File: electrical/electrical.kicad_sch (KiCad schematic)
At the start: 0 parts

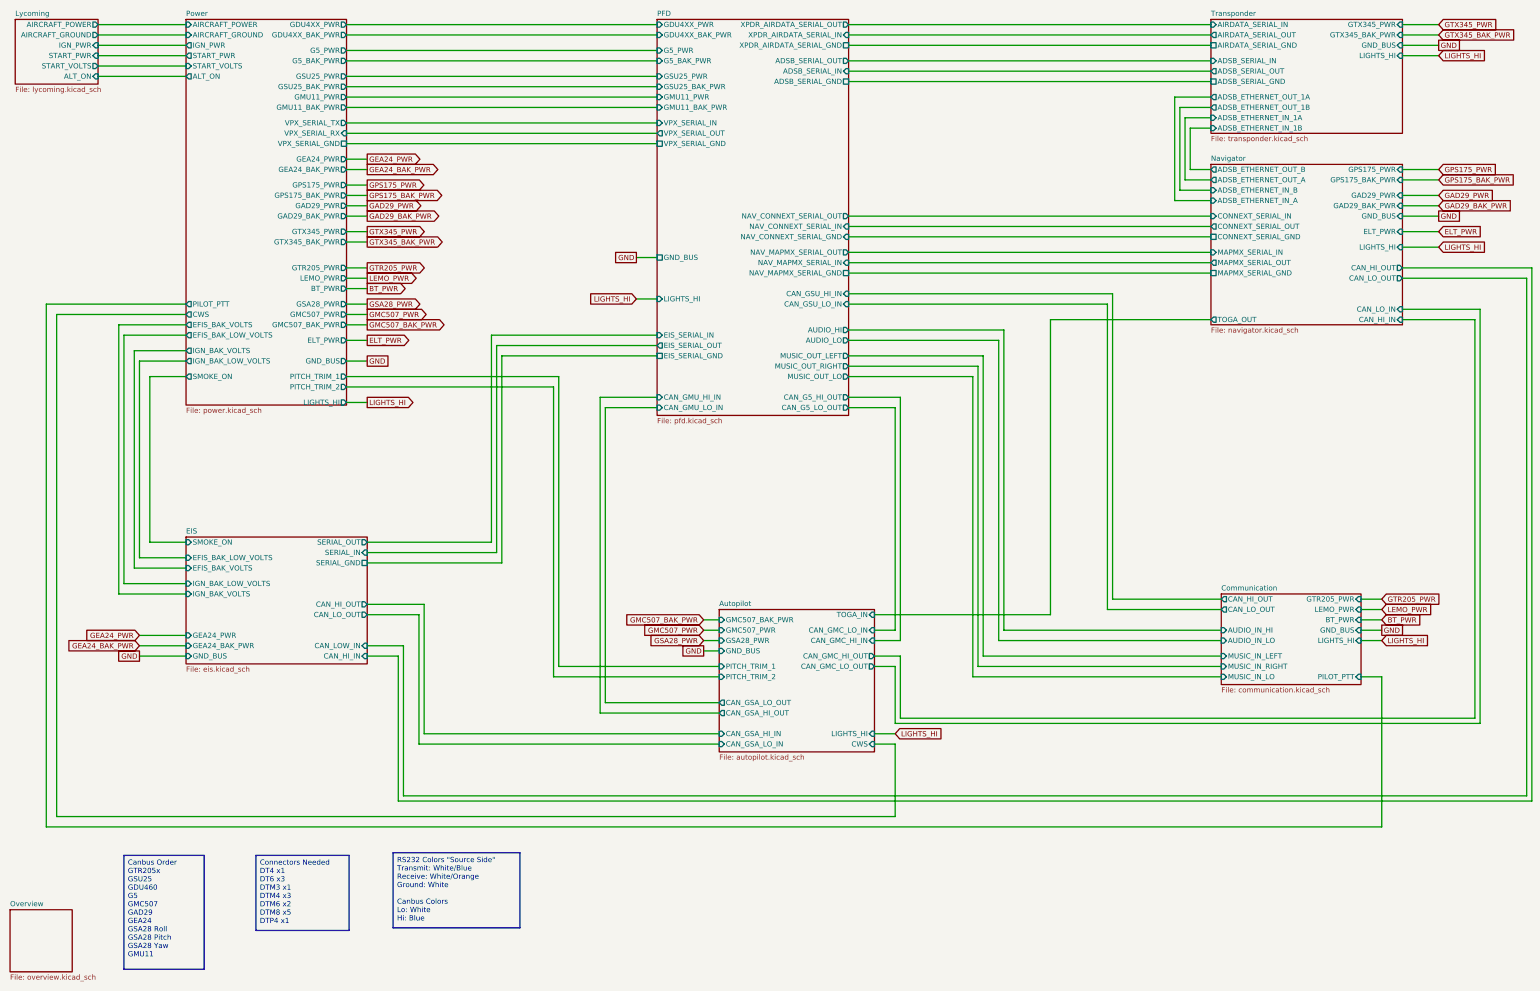
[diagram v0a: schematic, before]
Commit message: Added Rudder Trim and Ray Allen T3 Servo Type.
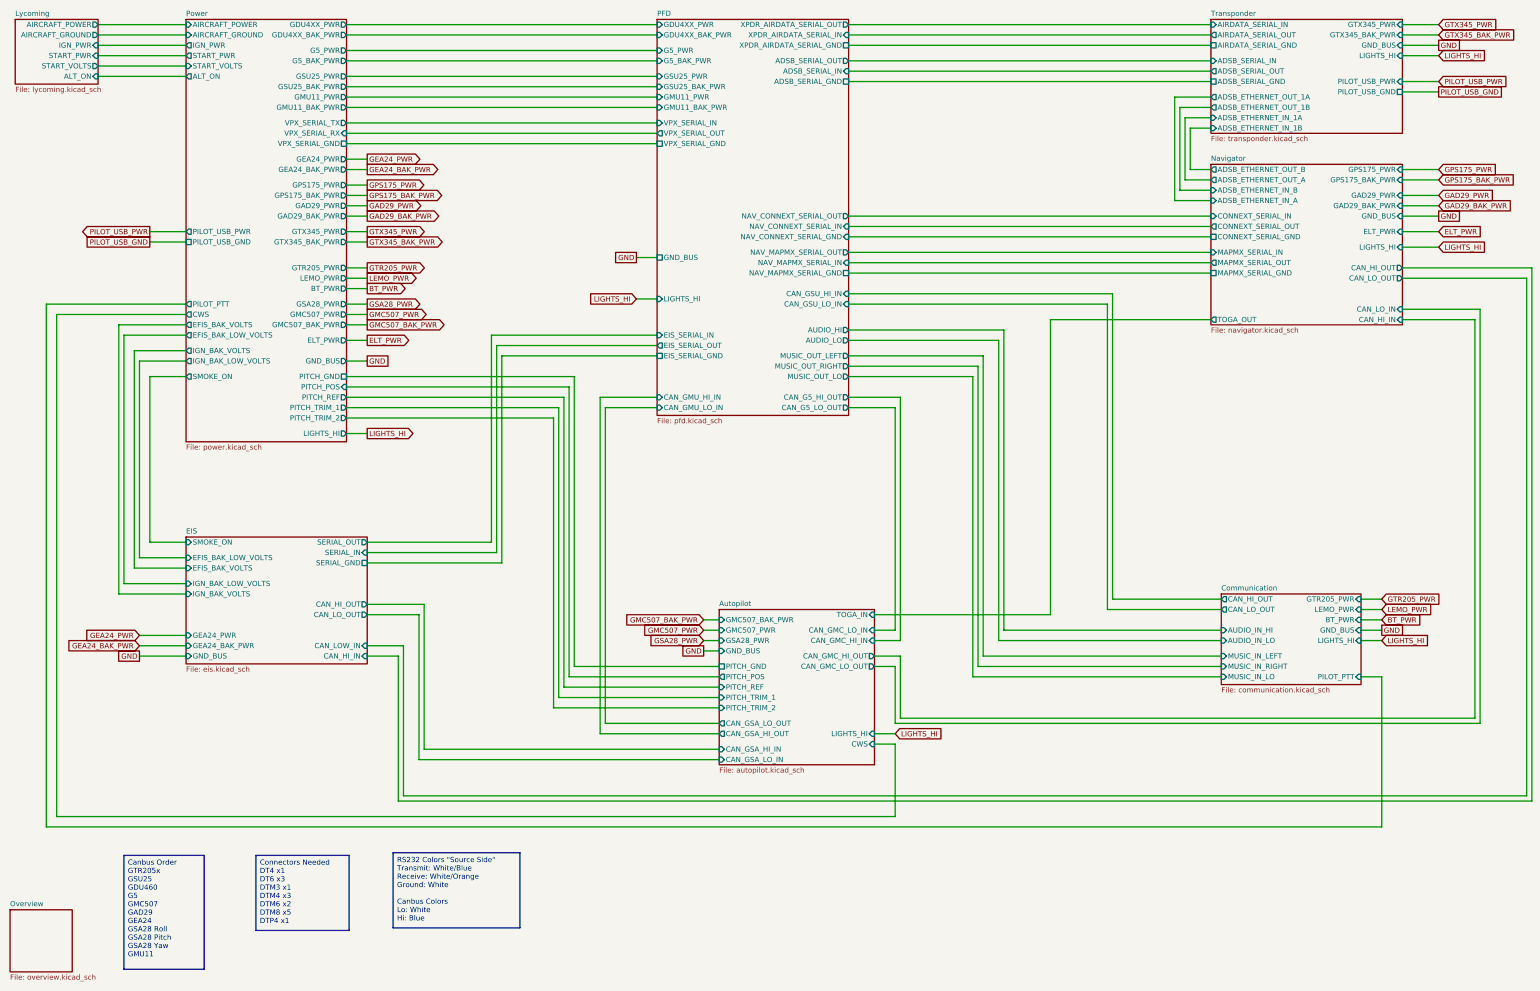
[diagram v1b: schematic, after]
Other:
- sheet Autopilot ports: added PITCH_GND, PITCH_POS, PITCH_REF; removed none
- sheet Power ports: added PILOT_USB_GND, PILOT_USB_PWR, PITCH_GND, PITCH_POS, PITCH_REF; removed none
- sheet Transponder ports: added PILOT_USB_GND, PILOT_USB_PWR; removed none

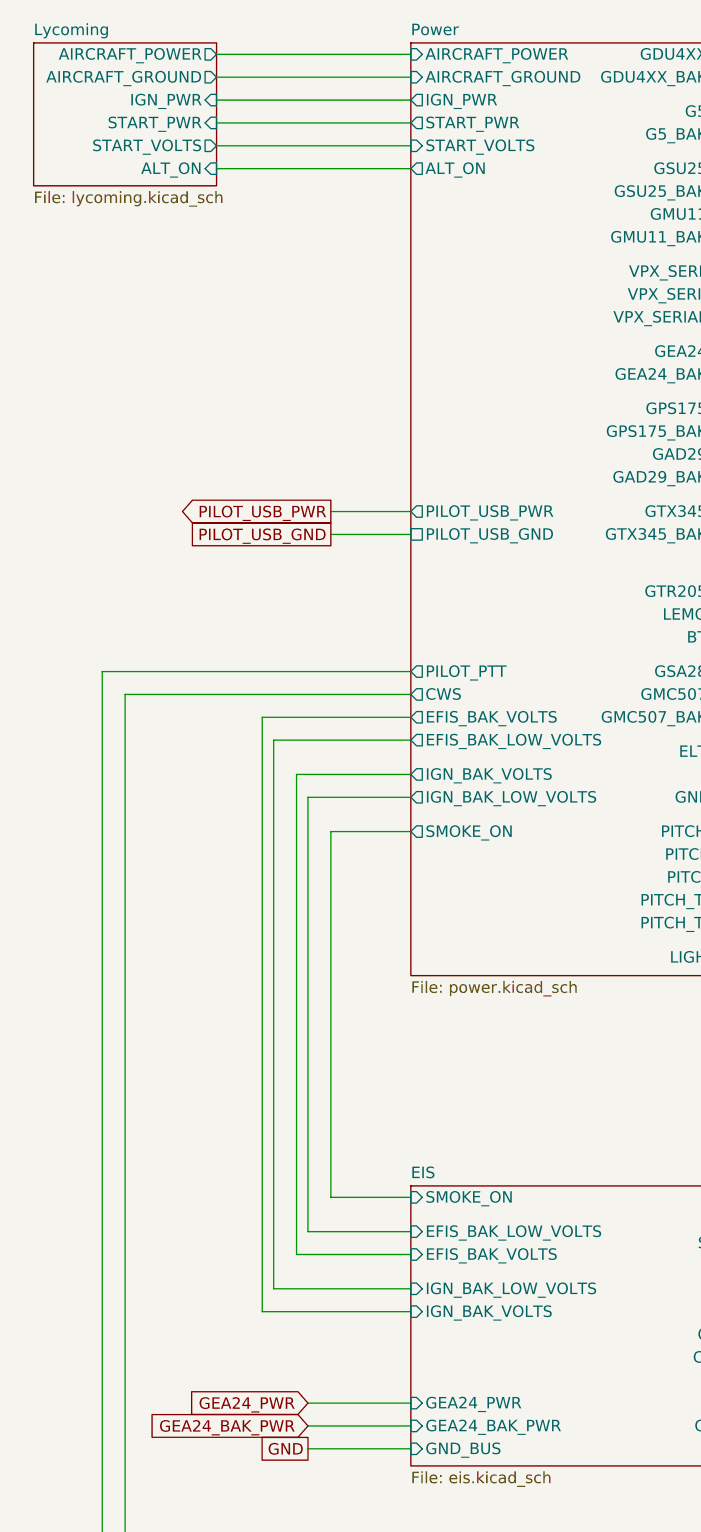
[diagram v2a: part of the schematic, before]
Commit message: adds battery fault
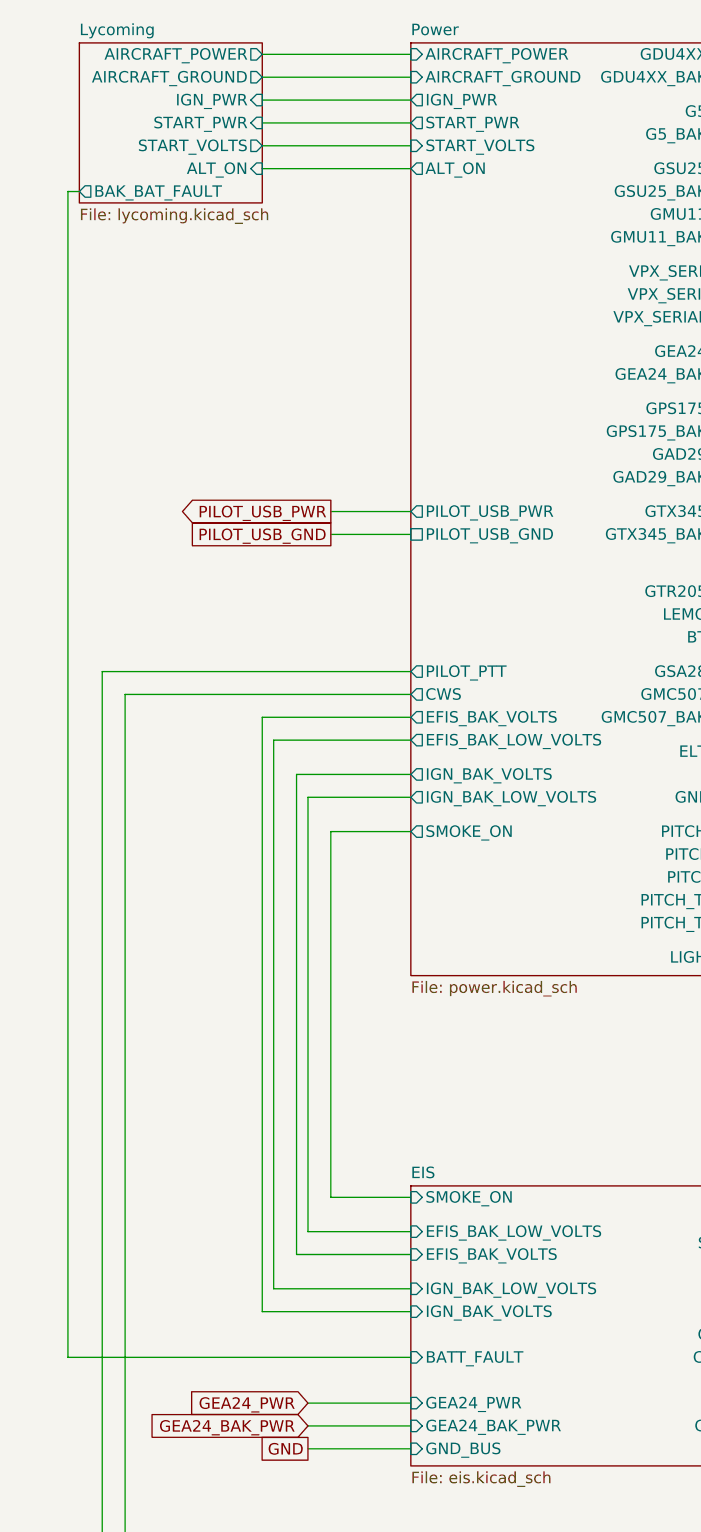
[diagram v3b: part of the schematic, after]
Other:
- sheet EIS ports: added BATT_FAULT; removed none
- sheet Lycoming ports: added BAK_BAT_FAULT; removed none
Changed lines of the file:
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@@
 	(title_block
 		(title "Electrical Overview")
-		(date "2025-11-19")
-		(rev "1.2.8")
+		(date "2026-04-02")
+		(rev "1.2.13")
 		(company "N78HR")
 	)
@@
 	(wire
 		(pts
-			(xy 36.83 33.02) (xy 58.42 33.02)
+			(xy 41.91 33.02) (xy 58.42 33.02)
 		)
 		(stroke
@@
 	(wire
 		(pts
-			(xy 36.83 43.18) (xy 58.42 43.18)
+			(xy 41.91 43.18) (xy 58.42 43.18)
 		)
 		(stroke
@@
 	(wire
 		(pts
-			(xy 36.83 40.64) (xy 58.42 40.64)
+			(xy 41.91 40.64) (xy 58.42 40.64)
 		)
 		(stroke
@@
 	(wire
 		(pts
+			(xy 20.32 45.72) (xy 20.32 175.26)
+		)
+		(stroke
+			(width 0)
+			(type default)
+		)
+	)
+	(wire
+		(pts
 			(xy 309.88 48.26) (xy 300.99 48.26)
 		)
@@
 	(wire
 		(pts
-			(xy 36.83 38.1) (xy 58.42 38.1)
+			(xy 41.91 38.1) (xy 58.42 38.1)
 		)
 		(stroke
@@
 	(wire
 		(pts
+			(xy 21.59 45.72) (xy 20.32 45.72)
+		)
+		(stroke
+			(width 0)
+			(type default)
+		)
+	)
+	(wire
+		(pts
 			(xy 284.48 173.99) (xy 312.42 173.99)
 		)
@@
 	(wire
 		(pts
-			(xy 36.83 35.56) (xy 58.42 35.56)
+			(xy 41.91 35.56) (xy 58.42 35.56)
 		)
 		(stroke
@@
 	(wire
 		(pts
-			(xy 36.83 30.48) (xy 58.42 30.48)
+			(xy 41.91 30.48) (xy 58.42 30.48)
 		)
 		(stroke
@@
 	(wire
 		(pts
+			(xy 20.32 175.26) (xy 58.42 175.26)
+		)
+		(stroke
+			(width 0)
+			(type default)
+		)
+	)
+	(wire
+		(pts
 			(xy 111.76 182.88) (xy 102.87 182.88)
 		)
@@
 	)
 	(sheet
-		(at 16.51 29.21)
-		(size 20.32 15.875)
+		(at 21.59 29.21)
+		(size 20.32 17.78)
 		(exclude_from_sim no)
 		(in_bom yes)
@@
 		)
 		(property "Sheetname" "Lycoming"
-			(at 16.51 28.4984 0)
+			(at 21.59 28.4984 0)
 			(effects
 				(font
@@
 		)
 		(property "Sheetfile" "lycoming.kicad_sch"
-			(at 16.51 45.6696 0)
+			(at 21.59 47.5746 0)
 			(effects
 				(font
@@
 		)
 		(pin "AIRCRAFT_POWER" output
-			(at 36.83 30.48 0)
+			(at 41.91 30.48 0)
 			(effects
 				(font
@@
 		)
 		(pin "AIRCRAFT_GROUND" output
-			(at 36.83 33.02 0)
+			(at 41.91 33.02 0)
 			(effects
 				(font
@@
 		)
 		(pin "IGN_PWR" input
-			(at 36.83 35.56 0)
+			(at 41.91 35.56 0)
 			(effects
 				(font
@@
 		)
 		(pin "START_PWR" input
-			(at 36.83 38.1 0)
+			(at 41.91 38.1 0)
 			(effects
 				(font
@@
 		)
 		(pin "START_VOLTS" output
-			(at 36.83 40.64 0)
+			(at 41.91 40.64 0)
 			(effects
 				(font
@@
 		)
 		(pin "ALT_ON" input
-			(at 36.83 43.18 0)
+			(at 41.91 43.18 0)
 			(effects
 				(font
@@
 			)
 		)
+		(pin "BAK_BAT_FAULT" output
+			(at 21.59 45.72 180)
+			(effects
+				(font
+					(size 1.27 1.27)
+				)
+				(justify left)
+			)
+		)
 		(instances
 			(project "electrical"
@@
 			)
 		)
+		(pin "BATT_FAULT" input
+			(at 58.42 175.26 180)
+			(effects
+				(font
+					(size 1.27 1.27)
+				)
+				(justify left)
+			)
+		)
